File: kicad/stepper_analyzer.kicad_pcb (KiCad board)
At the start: 2 copper layers, 102 x 57 mm, 23 parts, among them J1 Connector_Conn_01x04_Male, J2 Connector_Conn_01x04_Male, M1 Motor, Q1 AO3400A, U1 ACS70331EOLCTR-2P5B3, U2 ACS70331EOLCTR-2P5B3, U3 Pico

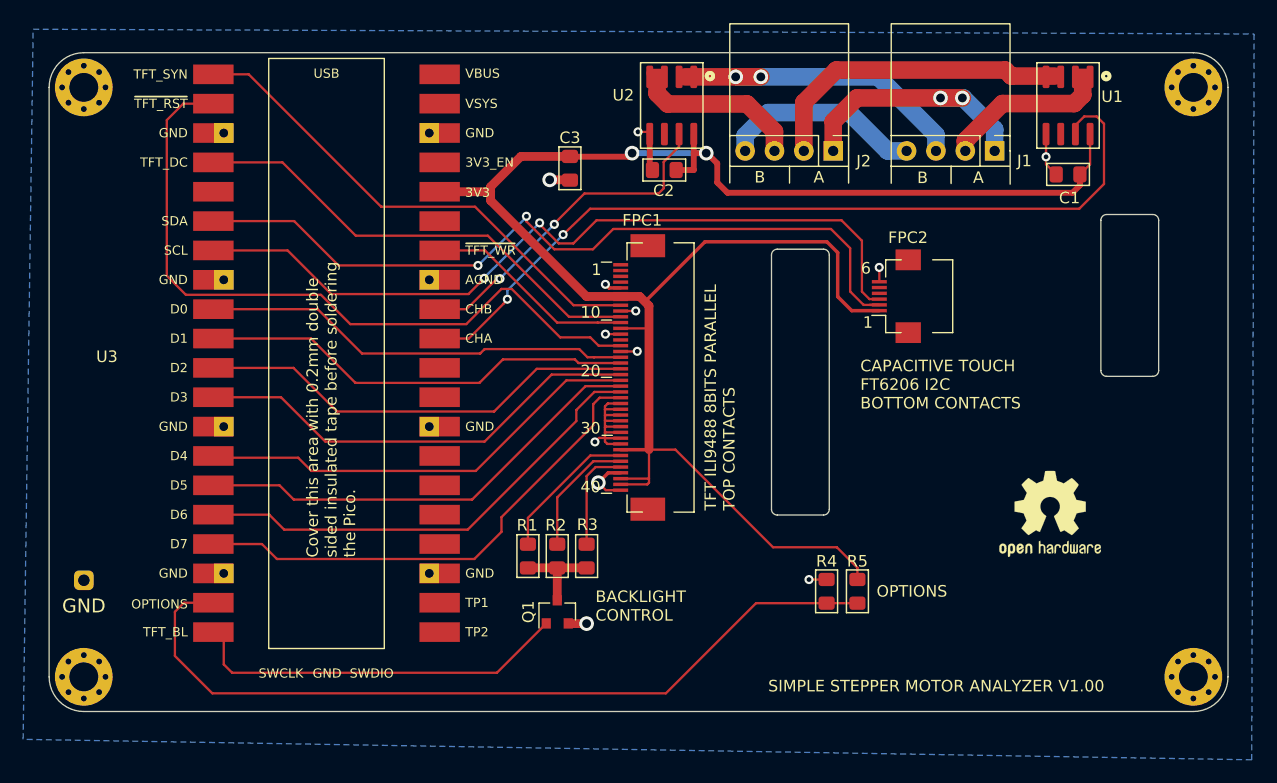
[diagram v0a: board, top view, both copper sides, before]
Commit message: Update before Etsy
Updated code and hardware for Th0mpy's version of the analyzer
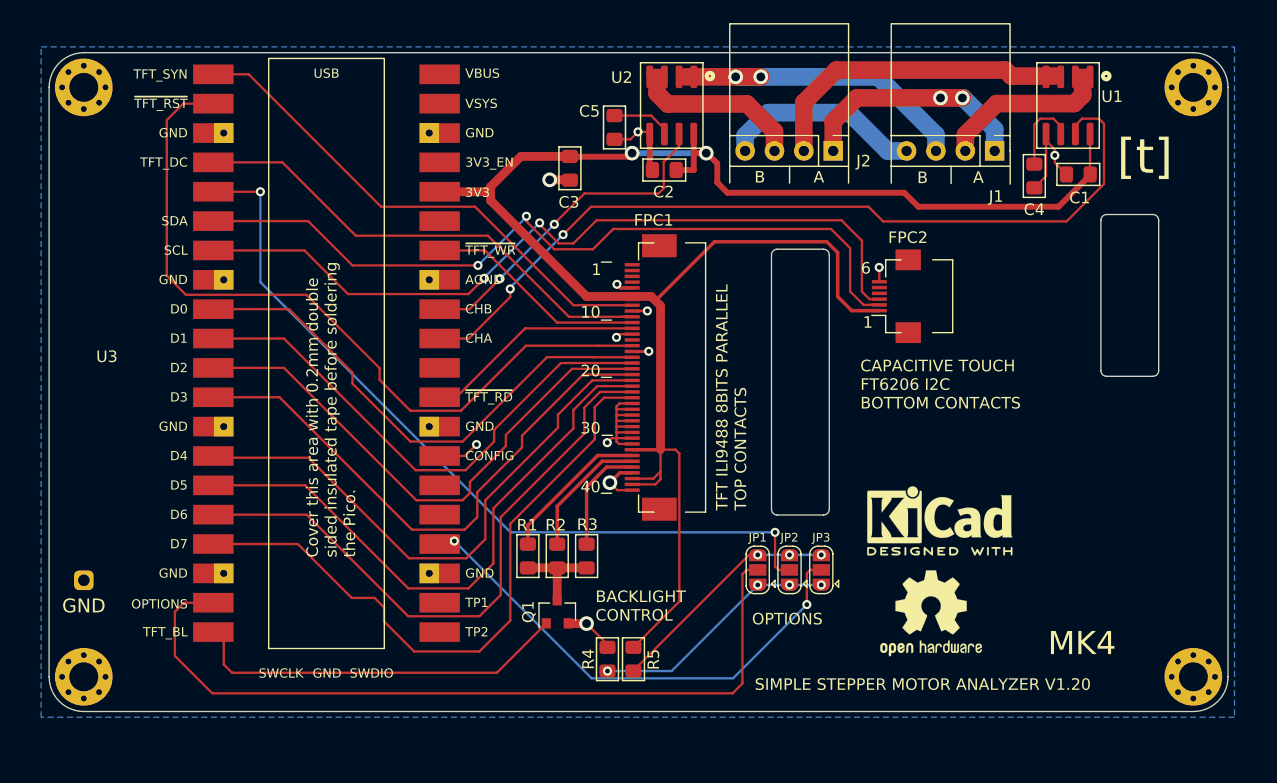
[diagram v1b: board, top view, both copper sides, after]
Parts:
- added C4: 1nf, stepper_motor_analyzer:C_0805_2012Metric_Pad1.15x1.40mm_HandSolder, F.Cu at (84.2, -46.3)
- added C5: DNP, stepper_motor_analyzer:C_0805_2012Metric_Pad1.15x1.40mm_HandSolder, F.Cu at (47.9, -50.5)
- added JP1: OPTION1, Jumper:SolderJumper-3_P1.3mm_Open_RoundedPad1.0x1.5mm, F.Cu at (60.3, -12.2)
- added JP2: OPTION2, Jumper:SolderJumper-3_P1.3mm_Open_RoundedPad1.0x1.5mm, F.Cu at (63.1, -12.2)
- added JP3: OPTION3, Jumper:SolderJumper-3_P1.3mm_Open_RoundedPad1.0x1.5mm, F.Cu at (65.8, -12.2)
- added REF**: KiCad-Logo2_5mm_SilkScreen, Symbol:KiCad-Logo2_5mm_SilkScreen, F.Cu at (76.1, -16.5)
- R4: value DNP -> 1K; footprint stepper_motor_analyzer:R_0805_2012Metric_Pad1.15x1.40mm_HandSolder_no_3d -> stepper_motor_analyzer:R_0805_2012Metric_Pad1.15x1.40mm_HandSolder
- R5: value DNP -> 1K
- U1, U2: value ACS70331EOLCTR-2P5B3 -> (CURRENT SENSOR)
- moved R5 20.2 mm to (49.6, -4.53)
- moved R4 19.8 mm to (47.3, -4.53)
- moved LOGO1 13.4 mm to (75.3, -8.50)
- moved FPC1 1.00 mm to (51.3, -28.9)
- moved C1 0.89 mm to (88.0, -46.5)
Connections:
- FPC1 pad 1: Net-(FPC1-Pad1) -> (no net)
- FPC1 pad 12: +3V3 -> /~TFT_RD
- FPC1 pad 14: Net-(FPC1-Pad14) -> (no net)
- FPC1 pad 2: Net-(FPC1-Pad2) -> (no net)
- FPC1 pad 3: Net-(FPC1-Pad3) -> (no net)
- FPC1 pad 4: Net-(FPC1-Pad4) -> (no net)
- FPC2 pad 4: Net-(FPC2-Pad4) -> (no net)
- FPC2 pad 5: Net-(FPC2-Pad5) -> (no net)
- R4 pad 1: /OPTIONS -> Net-(JP1-Pad1)
- R5 pad 1: /OPTIONS -> Net-(JP1-Pad3)
- U3 pad 19: /OPTIONS -> /OPTION1
- U3 pad 21: Net-(U3-Pad21) -> (no net)
- U3 pad 22: Net-(U3-Pad22) -> (no net)
- U3 pad 24: Net-(U3-Pad24) -> /OPTION3
- U3 pad 25: Net-(U3-Pad25) -> (no net)
- U3 pad 26: Net-(U3-Pad26) -> (no net)
- U3 pad 27: Net-(U3-Pad27) -> GND
- U3 pad 29: Net-(U3-Pad29) -> /~TFT_RD
- U3 pad 30: Net-(U3-Pad30) -> (no net)
- U3 pad 35: Net-(U3-Pad35) -> (no net)
- U3 pad 37: Net-(U3-Pad37) -> (no net)
- U3 pad 39: Net-(U3-Pad39) -> (no net)
- U3 pad 40: Net-(U3-Pad40) -> (no net)
- U3 pad 5: Net-(U3-Pad5) -> /OPTION2
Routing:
- net /OPTIONS: track 72.0 -> 0.00 mm
- net /OPTION1: track 0.00 -> 70.1 mm
- net /OPTION2: track 0.00 -> 68.8 mm, vias 0 -> 2
- net /OPTION3: track 0.00 -> 42.1 mm, vias 0 -> 2
- net Net-(JP1-Pad1): track 0.00 -> 21.6 mm, vias 0 -> 4
- net Net-(JP1-Pad3): track 0.00 -> 20.4 mm, vias 0 -> 3
- net /~TFT_RD: track 0.00 -> 20.3 mm
- net GND: track 39.3 -> 54.4 mm
- net /D7: track 42.5 -> 55.6 mm
- net /D6: track 40.4 -> 52.3 mm
- net /D5: track 38.9 -> 50.0 mm
- net /D4: track 38.1 -> 48.0 mm
- net /D3: track 38.3 -> 47.5 mm
- net /D2: track 37.4 -> 45.9 mm
- net /D1: track 36.9 -> 44.5 mm
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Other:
- board text added: "MK4"
- board text added: "SIMPLE STEPPER MOTOR ANALYZER V1.20"
- board text added: "[t]"
- board text removed: "SIMPLE STEPPER MOTOR ANALYZER V1.00"
